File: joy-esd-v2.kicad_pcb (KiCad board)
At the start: 2 copper layers, 16 x 11.3 mm, 4 parts, among them J1 DB9_Female, U1 ESDA6V3SC5, U2 ESDA6V3SC5

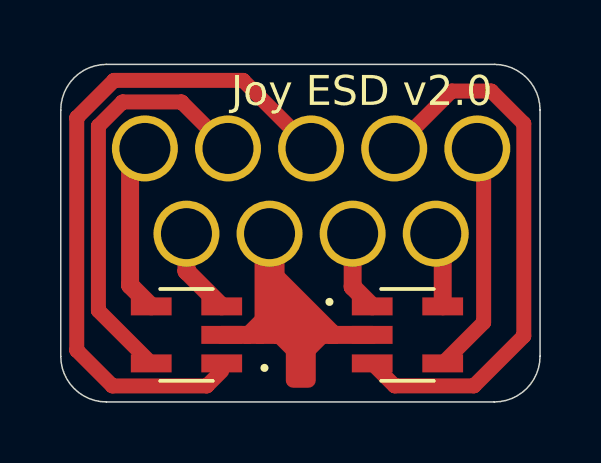
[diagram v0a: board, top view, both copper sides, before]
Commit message: Move from 5 to 6 pin SOT-23 diodes
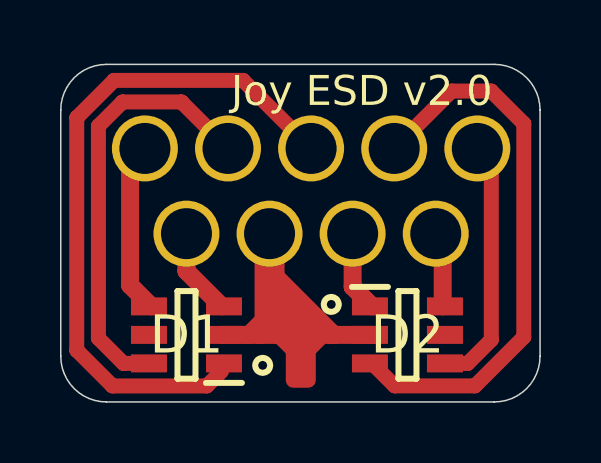
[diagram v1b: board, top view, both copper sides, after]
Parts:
- removed U1, U2: ESDA6V3SC5, ESDA5V3SC5:SOT95P280X145-5N
- added D1: ESDALD05UD4X, SamacSys:SOT95P280X125-6N, F.Cu at (152.1, 91.7)
- added D2: ESDALD05UD4X, SamacSys:SOT95P280X125-6N, F.Cu at (159.5, 91.7)
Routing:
- net Net-(D2-Pad4): track 7.82 -> 8.86 mm
- net Net-(D1-Pad6): track 13.9 -> 14.5 mm

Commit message: Add teardrops and ibom
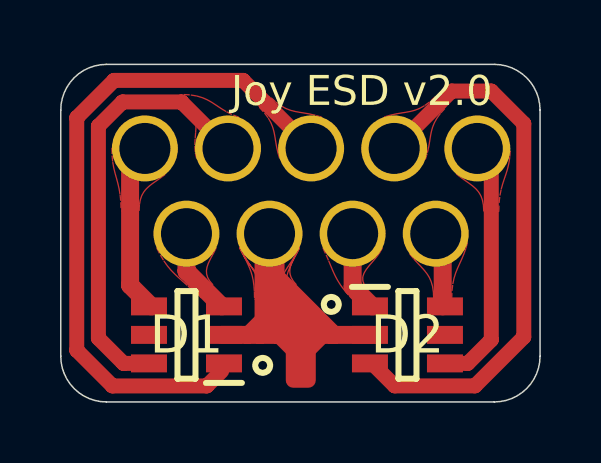
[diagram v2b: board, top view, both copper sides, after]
